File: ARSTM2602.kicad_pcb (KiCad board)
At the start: 2 copper layers, 100 x 100 mm, 62 parts, among them J1 Conn_01x02_Socket, J11 Conn_01x02_Socket, J12 Conn_01x02_Socket, J13 Conn_01x02_Socket, J3 USB_C_Receptacle_USB2.0_14P, J8 Conn_01x02_Socket, J9 Conn_ST_STDC14, SW1 SW_Push, SW2 SW_SPDT, SW3 SW_Push, SW4 SW_Push, SW5 SW_Wuerth_450301014042, SW6 SW_Wuerth_450301014042, U1 BD50FC0FP, U2 TCAN3414DRBR, U3 TCAN3414DRBR, U4 STM32H523CCTx, U5 BD33FC0FP, U6 ESP32-C3-WROOM-02, U7 BD33FC0FP, U8 RP2040, U9 CYW43439KUBGT

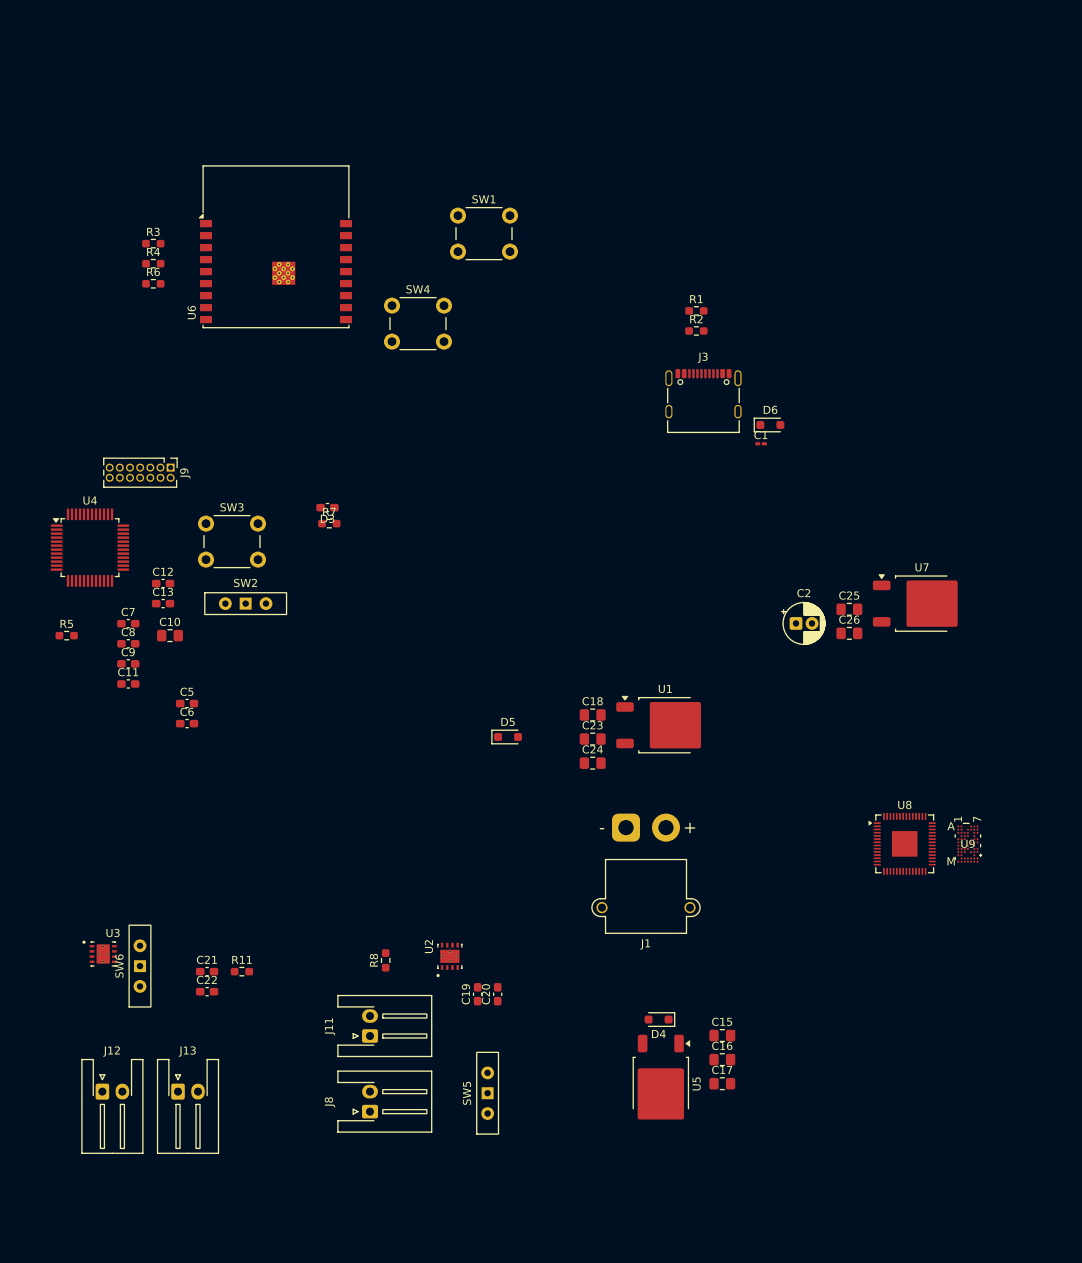
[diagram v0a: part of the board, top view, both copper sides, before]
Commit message: 一部回路図変更と部品配置
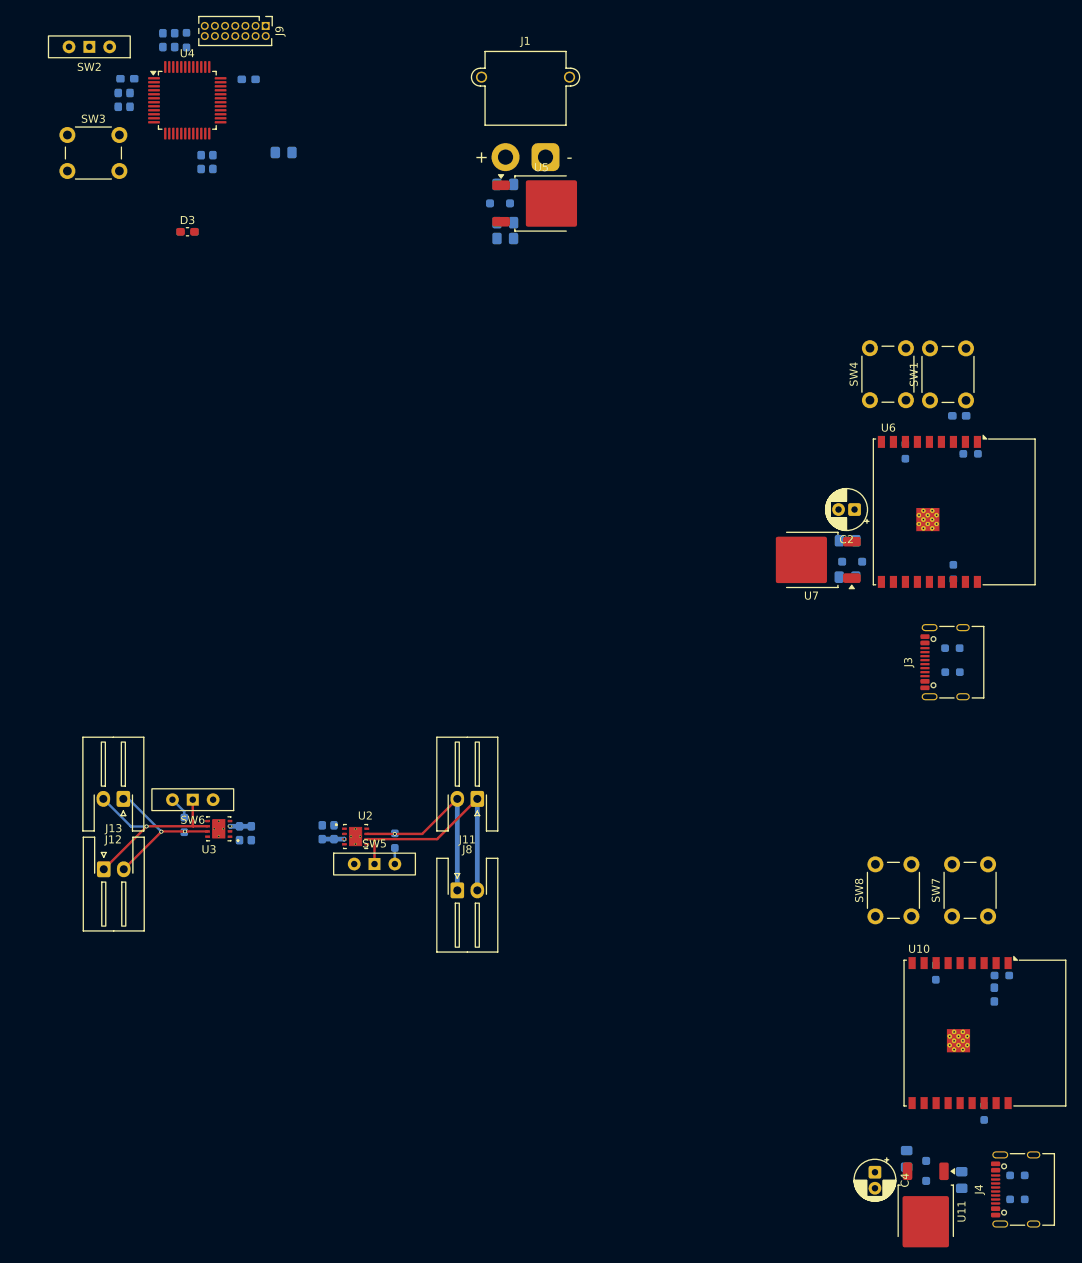
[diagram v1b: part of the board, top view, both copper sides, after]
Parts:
- removed C18, C23: 4.7μF, Capacitor_SMD:C_0805_2012Metric_Pad1.18x1.45mm_HandSolder
- removed C24: 22μF, Capacitor_SMD:C_0805_2012Metric_Pad1.18x1.45mm_HandSolder
- removed D5: D_Shockley, Diode_SMD:D_SOD-323_HandSoldering
- removed U1: BD50FC0FP, Package_TO_SOT_SMD:TO-252-2
- removed U8: RP2040, Package_DFN_QFN:QFN-56-1EP_7x7mm_P0.4mm_EP3.2x3.2mm
- removed U9: CYW43439KUBGT, cyw43439:SG-XFWLB-63-800
- added C27: 4.7μF, Capacitor_SMD:C_0805_2012Metric_Pad1.18x1.45mm_HandSolder, B.Cu at (273.0, 168.0)
- added C28: 4.7μF, Capacitor_SMD:C_0805_2012Metric_Pad1.18x1.45mm_HandSolder, B.Cu at (266.1, 165.4)
- added C3: 1uf, Capacitor_SMD:C_0603_1608Metric_Pad1.08x0.95mm_HandSolder, B.Cu at (277.0, 144.9)
- added C4: 22uf, Capacitor_THT:CP_Radial_D5.0mm_P2.00mm, F.Cu at (262.1, 167.1)
- added D7: D_Shockley, Diode_SMD:D_SOD-323_HandSoldering, B.Cu at (268.5, 166.9)
- added J4: USB_C_Receptacle_USB2.0_14P, Connector_USB:USB_C_Receptacle_Palconn_UTC16-G, F.Cu at (279.7, 169.2)
- added R10: 5.1k, Resistor_SMD:R_0603_1608Metric_Pad0.98x0.95mm_HandSolder, B.Cu at (279.9, 167.5)
- added R12: 10k, Resistor_SMD:R_0603_1608Metric_Pad0.98x0.95mm_HandSolder, B.Cu at (278.0, 142.5)
- added R13: 10k, Resistor_SMD:R_0603_1608Metric_Pad0.98x0.95mm_HandSolder, B.Cu at (275.8, 159.6)
- added R14: 10k, Resistor_SMD:R_0603_1608Metric_Pad0.98x0.95mm_HandSolder, B.Cu at (269.7, 142.1)
- added R9: 5.1k, Resistor_SMD:R_0603_1608Metric_Pad0.98x0.95mm_HandSolder, B.Cu at (279.9, 170.5)
- added SW7: SW_Push, Button_Switch_THT:SW_PUSH_6mm, F.Cu at (271.8, 135.1)
- added SW8: SW_Push, Button_Switch_THT:SW_PUSH_6mm, F.Cu at (262.2, 135.1)
- added U10: ESP32-C3-WROOM-02, RF_Module:ESP32-C3-WROOM-02, F.Cu at (272.8, 149.7)
- added U11: BD33FC0FP, Package_TO_SOT_SMD:TO-252-2, F.Cu at (268.5, 172.0)
- C1: footprint Capacitor_SMD:C_0201_0603Metric_Pad0.64x0.40mm_HandSolder -> Capacitor_SMD:C_0603_1608Metric_Pad1.08x0.95mm_HandSolder; moved to B.Cu
- C10, C11, C12, C13, C15, C16, C17, C19, C20, C21, C22, C25, C26, C5, C6, C7, C8, C9, D4, D6, R1, R11, R2, R3, R4, R5, R6, R7, R8: moved to B.Cu
- moved U5 111.1 mm to (220.4, 46.0), turned to 0 degrees
- moved C15 109.8 mm to (215.9, 43.6)
- moved C17 109.1 mm to (215.9, 50.4)
- moved R3 108.1 mm to (271.9, 92.1), turned to 90 degrees
- moved C16 108.1 mm to (215.9, 48.4)
- moved R6 104.4 mm to (274.1, 77.3)
- moved D4 103.9 mm to (215.2, 46.0)
- moved R4 96.9 mm to (265.9, 77.0), turned to -90 degrees
- moved U6 87.0 mm to (268.9, 84.5), turned to -90 degrees
- moved C6 85.4 mm to (174.6, 25.6), turned to -90 degrees
- moved J1 84.4 mm to (220.9, 40.2), turned to 0 degrees
- moved C11 80.6 mm to (173.1, 25.6), turned to 90 degrees
- moved R5 75.9 mm to (176.1, 25.6), turned to 90 degrees
- moved C9 74.6 mm to (183.8, 30.5)
- moved SW2 72.3 mm to (163.9, 26.4), turned to 180 degrees
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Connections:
- C15 pad 1: +5V -> +24V
- D4 pad 1: +5V -> +24V
- J11 pad 1: CAN2_L -> CAN2_-
- J11 pad 2: CAN2_H -> CAN2_+
- J12 pad 1: CAN1_H -> CAN1_+
- J12 pad 2: CAN1_L -> CAN1_-
- J13 pad 1: CAN1_L -> CAN1_-
- J13 pad 2: CAN1_H -> CAN1_+
- J8 pad 1: CAN2_H -> CAN2_+
- J8 pad 2: CAN2_L -> CAN2_-
- R11 pad 1: CAN1_H -> CAN1_+
- R7 pad 1: unconnected-(R7-Pad1) -> GND
- R8 pad 1: CAN2_H -> CAN2_+
- SW5 pad 1: CAN2_H -> CAN2_-
- SW6 pad 1: CAN1_H -> CAN1_-
- U2 pad 6: CAN2_L -> CAN2_-
- U2 pad 7: CAN2_H -> CAN2_+
- U3 pad 6: CAN1_L -> CAN1_-
- U3 pad 7: CAN1_H -> CAN1_+
- U5 pad 1: +5V -> +24V
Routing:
- net CAN2_-: track 0.00 -> 30.4 mm
- net CAN1_-: track 0.00 -> 25.4 mm, vias 0 -> 1
- net CAN2_+: track 0.00 -> 24.6 mm, vias 0 -> 1
- net CAN1_+: track 0.00 -> 18.9 mm, vias 0 -> 2
- net +3.3V: track 0.00 -> 5.44 mm, vias 0 -> 2
- net CAN1R: track 0.00 -> 2.85 mm
- net CAN2R: track 0.00 -> 2.01 mm

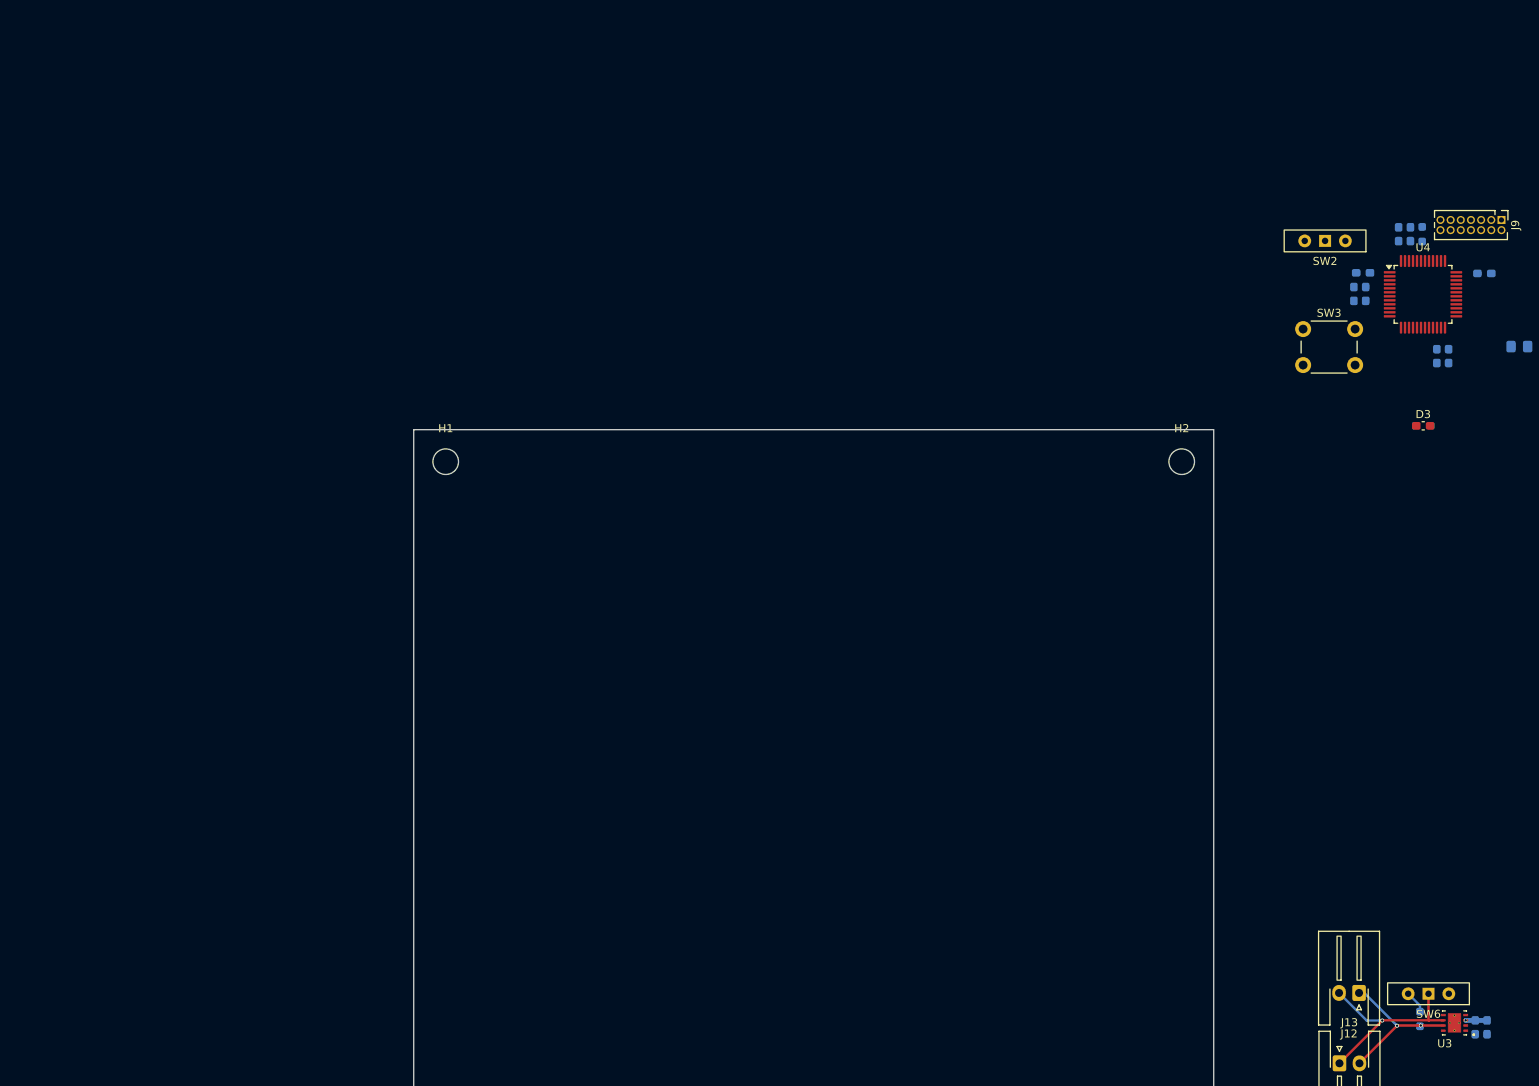
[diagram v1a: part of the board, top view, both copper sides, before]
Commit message: 電磁弁用回路の増設
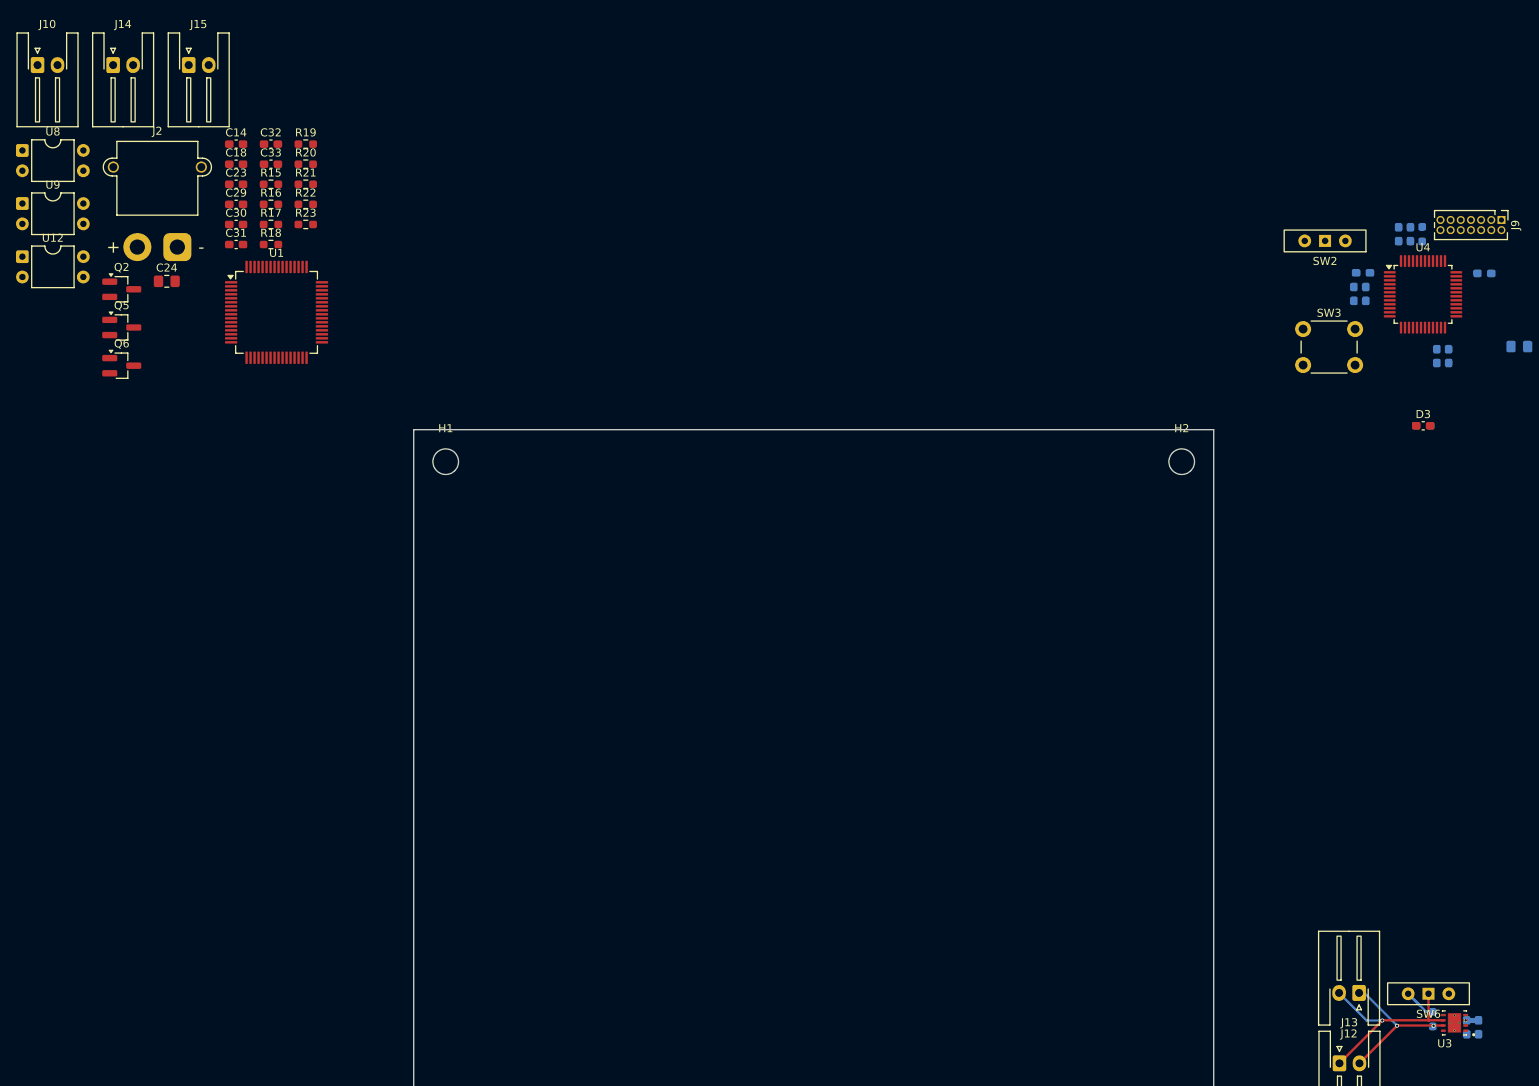
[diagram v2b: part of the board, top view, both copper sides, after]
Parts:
- added C14: 0.1uF, Capacitor_SMD:C_0603_1608Metric_Pad1.08x0.95mm_HandSolder, F.Cu at (27.8, 14.3)
- added C18: 0.1uF, Capacitor_SMD:C_0603_1608Metric_Pad1.08x0.95mm_HandSolder, F.Cu at (27.8, 16.8)
- added C23: 0.1uF, Capacitor_SMD:C_0603_1608Metric_Pad1.08x0.95mm_HandSolder, F.Cu at (27.8, 19.3)
- added C24: 4.7uf, Capacitor_SMD:C_0805_2012Metric_Pad1.18x1.45mm_HandSolder, F.Cu at (19.1, 31.5)
- added C29: 0.1uF, Capacitor_SMD:C_0603_1608Metric_Pad1.08x0.95mm_HandSolder, F.Cu at (27.8, 21.8)
- added C30: 0.1uf, Capacitor_SMD:C_0603_1608Metric_Pad1.08x0.95mm_HandSolder, F.Cu at (27.8, 24.3)
- added C31: 1uf, Capacitor_SMD:C_0603_1608Metric_Pad1.08x0.95mm_HandSolder, F.Cu at (27.8, 26.9)
- added C32: 0.1uF, Capacitor_SMD:C_0603_1608Metric_Pad1.08x0.95mm_HandSolder, F.Cu at (32.2, 14.3)
- added C33: 1uf, Capacitor_SMD:C_0603_1608Metric_Pad1.08x0.95mm_HandSolder, F.Cu at (32.2, 16.8)
- added J10: Conn_01x02_Socket, Connector_JST:JST_XH_S2B-XH-A-1_1x02_P2.50mm_Horizontal, F.Cu at (2.98, 4.42)
- added J14: Conn_01x02_Socket, Connector_JST:JST_XH_S2B-XH-A-1_1x02_P2.50mm_Horizontal, F.Cu at (12.4, 4.42)
- added J15: Conn_01x02_Socket, Connector_JST:JST_XH_S2B-XH-A-1_1x02_P2.50mm_Horizontal, F.Cu at (21.9, 4.42)
- added J2: Conn_01x02_Socket, Connector_AMASS:AMASS_XT30PW-M_1x02_P2.50mm_Horizontal, F.Cu at (20.5, 27.2)
- added Q2: Q_NMOS_GSD, Package_TO_SOT_SMD:SOT-23_Handsoldering, F.Cu at (13.5, 32.5)
- added Q5: Q_NMOS_GSD, Package_TO_SOT_SMD:SOT-23_Handsoldering, F.Cu at (13.5, 37.2)
- added Q6: Q_NMOS_GSD, Package_TO_SOT_SMD:SOT-23_Handsoldering, F.Cu at (13.5, 42.0)
- added R15: 330, Resistor_SMD:R_0603_1608Metric_Pad0.98x0.95mm_HandSolder, F.Cu at (32.2, 19.3)
- added R16: 10k, Resistor_SMD:R_0603_1608Metric_Pad0.98x0.95mm_HandSolder, F.Cu at (32.2, 21.8)
- added R17: 330, Resistor_SMD:R_0603_1608Metric_Pad0.98x0.95mm_HandSolder, F.Cu at (32.2, 24.3)
- added R18: 10k, Resistor_SMD:R_0603_1608Metric_Pad0.98x0.95mm_HandSolder, F.Cu at (32.2, 26.9)
- added R19: 330, Resistor_SMD:R_0603_1608Metric_Pad0.98x0.95mm_HandSolder, F.Cu at (36.5, 14.3)
- added R20: 10k, Resistor_SMD:R_0603_1608Metric_Pad0.98x0.95mm_HandSolder, F.Cu at (36.5, 16.8)
- added R21: 10k, Resistor_SMD:R_0603_1608Metric_Pad0.98x0.95mm_HandSolder, F.Cu at (36.5, 19.3)
- added R22: 10k, Resistor_SMD:R_0603_1608Metric_Pad0.98x0.95mm_HandSolder, F.Cu at (36.5, 21.8)
- added R23: 10k, Resistor_SMD:R_0603_1608Metric_Pad0.98x0.95mm_HandSolder, F.Cu at (36.5, 24.3)
- added U1: STM32G431RBTx, Package_QFP:LQFP-64_10x10mm_P0.5mm, F.Cu at (32.9, 35.3)
- added U12: TLP785, Package_DIP:DIP-4_W7.62mm, F.Cu at (1.08, 28.4)
- added U8: TLP785, Package_DIP:DIP-4_W7.62mm, F.Cu at (1.08, 15.1)
- added U9: TLP785, Package_DIP:DIP-4_W7.62mm, F.Cu at (1.08, 21.7)
- moved R11 1.60 mm to (177.4, 123.7)
- moved C21 1.07 mm to (183.1, 124.7)
- moved C22 1.07 mm to (181.6, 124.7)
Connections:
- U4 pad 21: /scl -> unconnected-(U4-PB10-Pad21)
- U4 pad 25: /sda -> CAN2rx
- U4 pad 26: unconnected-(U4-PB13-Pad26) -> CAN2tx
- U4 pad 32: unconnected-(U4-PA11-Pad32) -> CAN1rx
- U4 pad 33: unconnected-(U4-PA12-Pad33) -> CAN1tx
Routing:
- net CAN1R: track 2.85 -> 6.09 mm
- net +3.3V: track 5.44 -> 4.24 mm
